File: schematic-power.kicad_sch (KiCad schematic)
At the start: 25 parts, among them IC2 LM76202QPWPRQ1, U9 TPS62933

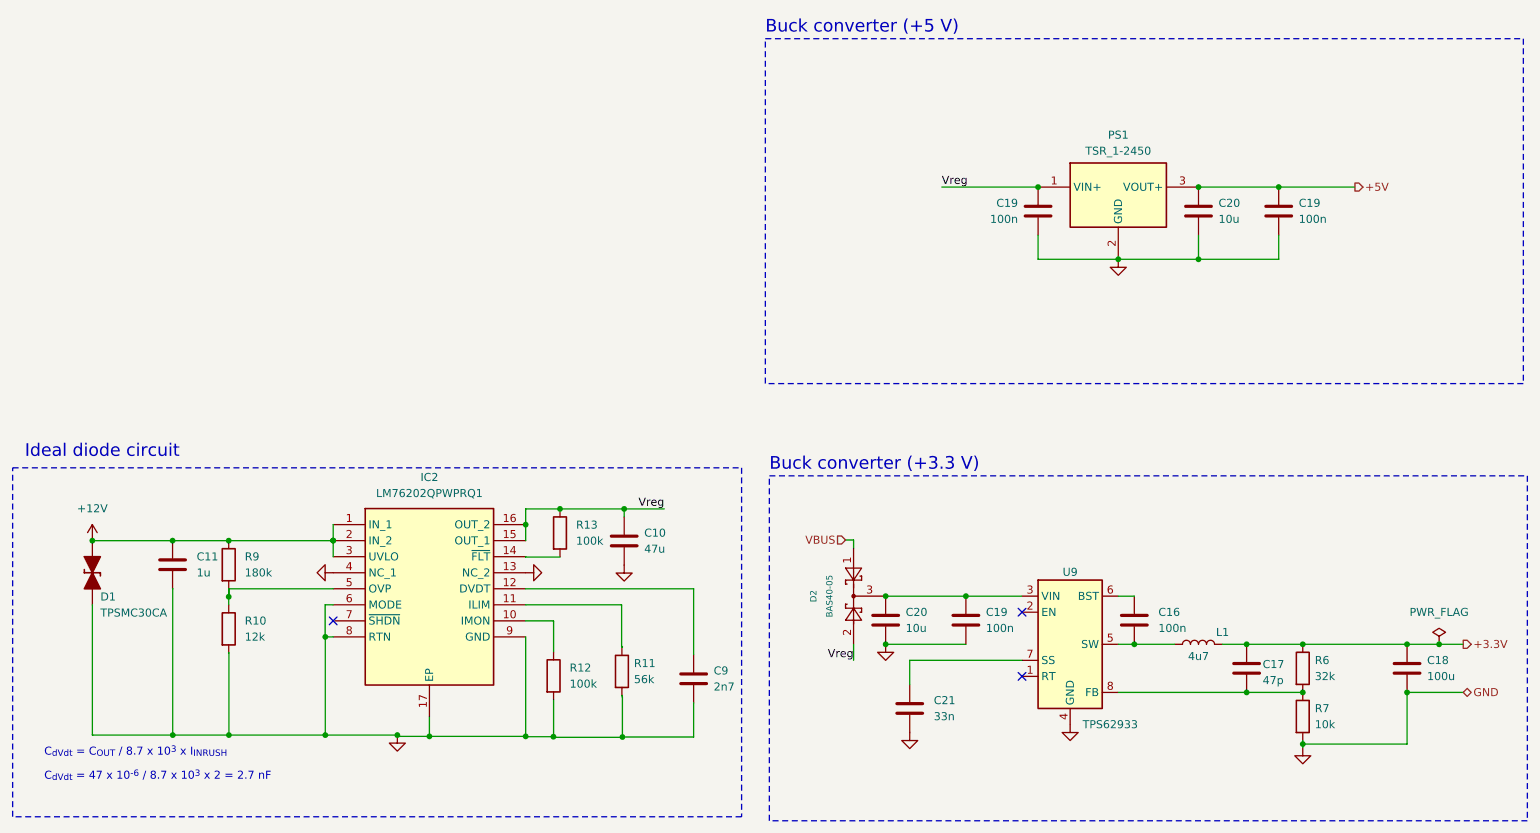
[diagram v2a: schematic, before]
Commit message: Edit mosfets outputs
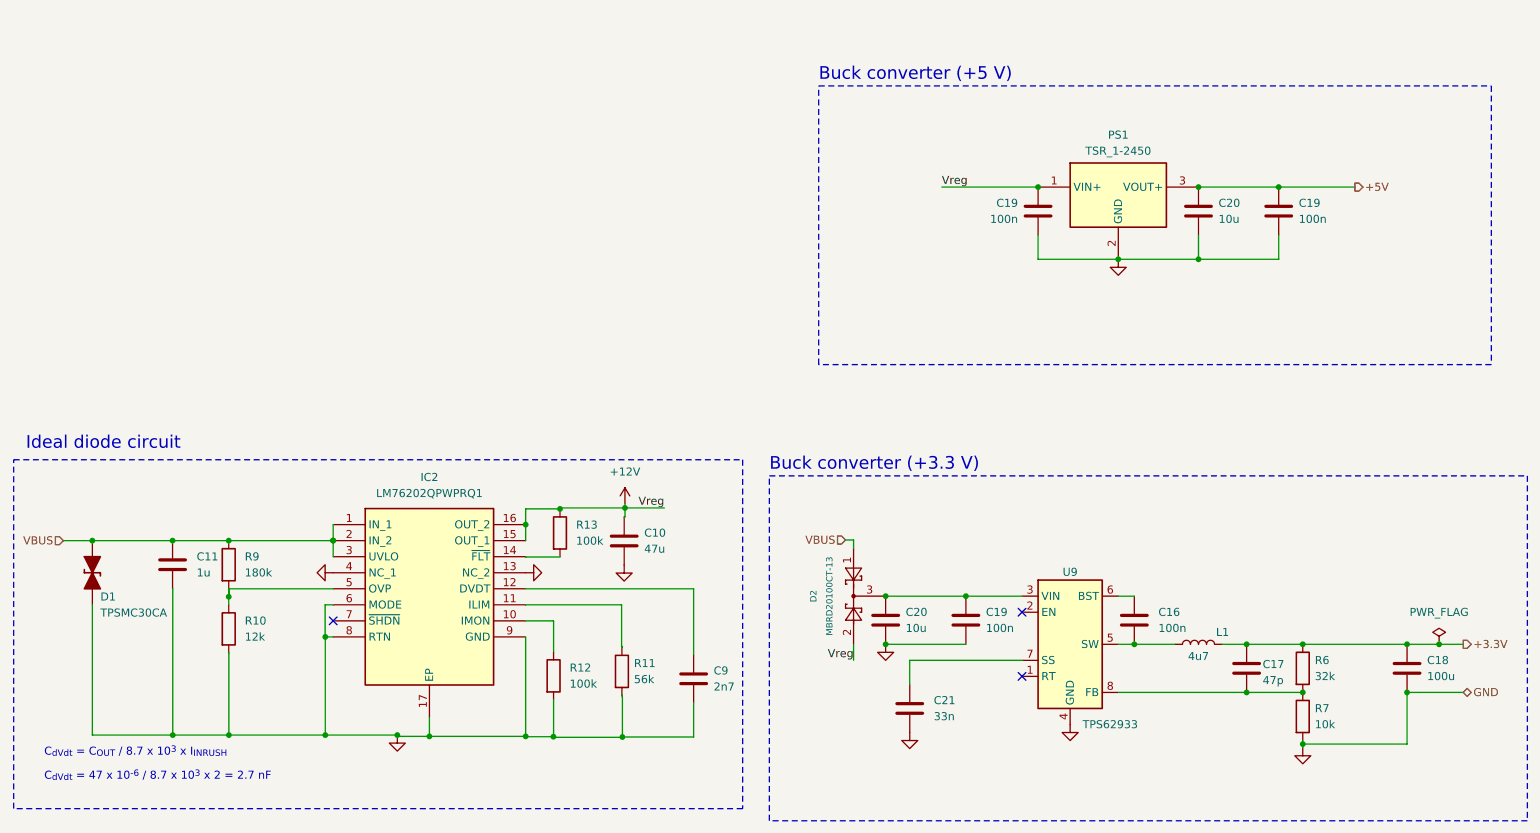
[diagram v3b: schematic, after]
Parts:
- D2: value BAS40-05 -> MBRD20100CT-13; footprint Package_TO_SOT_SMD:SOT-23 -> MBRD20100CT-13:TO252_(DPAK)_1
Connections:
- net Vreg is gone; now on net +12V: C10.1, C19.1, D2.2, IC2.15 (OUT_1), IC2.16 (OUT_2), PS1.1 (VIN+), R13.1
- net +12V: no longer C11.1, D1.2 (A), IC2.1 (IN_1), IC2.2 (IN_2), IC2.3 (UVLO), R9.1
- net VBUS: now also C11.1, D1.2 (A), IC2.1 (IN_1), IC2.2 (IN_2), IC2.3 (UVLO), R9.1
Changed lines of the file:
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@@
   (junction (at 215.9 64.77) (diameter 0) (color 0 0 0 0)
   )
+  (junction (at 203.2 64.77) (diameter 0) (color 0 0 0 0)
+  )
+  (junction (at 62.357 118.2116) (diameter 0) (color 0 0 0 0)
+  )
+  (junction (at 223.52 133.35) (diameter 0) (color 0 0 0 0)
+  )
+  (junction (at 53.467 109.3216) (diameter 0) (color 0 0 0 0)
+  )
+  (junction (at 215.9 53.34) (diameter 0) (color 0 0 0 0)
+  )
+  (junction (at 248.92 133.35) (diameter 0) (color 0 0 0 0)
+  )
+  (junction (at 77.6478 140.1064) (diameter 0) (color 0 0 0 0)
+  )
+  (junction (at 89.0524 140.1064) (diameter 0) (color 0 0 0 0)
+  )
+  (junction (at 78.8924 109.3216) (diameter 0) (color 0 0 0 0)
+  )
+  (junction (at 62.3824 140.1064) (diameter 0) (color 0 0 0 0)
+  )
+  (junction (at 232.41 133.35) (diameter 0) (color 0 0 0 0)
+  )
+  (junction (at 109.3724 106.7816) (diameter 0) (color 0 0 0 0)
+  )
+  (junction (at 190.5 53.34) (diameter 0) (color 0 0 0 0)
+  )
+  (junction (at 166.37 118.11) (diameter 0) (color 0 0 0 0)
+  )
+  (junction (at 205.74 125.73) (diameter 0) (color 0 0 0 0)
+  )
+  (junction (at 124.6886 140.4112) (diameter 0) (color 0 0 0 0)
+  )
+  (junction (at 248.92 125.73) (diameter 0) (color 0 0 0 0)
+  )
   (junction (at 40.767 109.3216) (diameter 0) (color 0 0 0 0)
   )
-  (junction (at 203.2 64.77) (diameter 0) (color 0 0 0 0)
-  )
-  (junction (at 62.357 118.2116) (diameter 0) (color 0 0 0 0)
-  )
-  (junction (at 223.52 133.35) (diameter 0) (color 0 0 0 0)
-  )
-  (junction (at 53.467 109.3216) (diameter 0) (color 0 0 0 0)
-  )
-  (junction (at 215.9 53.34) (diameter 0) (color 0 0 0 0)
-  )
-  (junction (at 248.92 133.35) (diameter 0) (color 0 0 0 0)
-  )
-  (junction (at 77.6478 140.1064) (diameter 0) (color 0 0 0 0)
-  )
-  (junction (at 89.0524 140.1064) (diameter 0) (color 0 0 0 0)
-  )
-  (junction (at 78.8924 109.3216) (diameter 0) (color 0 0 0 0)
-  )
-  (junction (at 62.3824 140.1064) (diameter 0) (color 0 0 0 0)
-  )
-  (junction (at 232.41 133.35) (diameter 0) (color 0 0 0 0)
-  )
-  (junction (at 109.3724 106.7816) (diameter 0) (color 0 0 0 0)
-  )
-  (junction (at 190.5 53.34) (diameter 0) (color 0 0 0 0)
-  )
-  (junction (at 166.37 118.11) (diameter 0) (color 0 0 0 0)
-  )
-  (junction (at 205.74 125.73) (diameter 0) (color 0 0 0 0)
-  )
-  (junction (at 124.6886 140.4112) (diameter 0) (color 0 0 0 0)
-  )
-  (junction (at 248.92 125.73) (diameter 0) (color 0 0 0 0)
-  )
-  (junction (at 124.968 104.2924) (diameter 0) (color 0 0 0 0)
+  (junction (at 125.095 104.14) (diameter 0) (color 0 0 0 0)
   )
   (junction (at 179.07 118.11) (diameter 0) (color 0 0 0 0)
@@
     (stroke (width 0) (type default))
   )
-  (wire (pts (xy 124.968 104.2924) (xy 131.318 104.2924))
+  (wire (pts (xy 125.095 104.14) (xy 131.318 104.14))
     (stroke (width 0) (type default))
   )
@@
     (stroke (width 0) (type default))
   )
+  (wire (pts (xy 125.095 105.5624) (xy 124.968 105.5624))
+    (stroke (width 0) (type default))
+  )
   (wire (pts (xy 124.6886 140.462) (xy 124.6886 140.4112))
     (stroke (width 0) (type default))
@@
     (stroke (width 0) (type default))
   )
+  (wire (pts (xy 125.095 103.505) (xy 125.095 104.14))
+    (stroke (width 0) (type default))
+  )
   (wire (pts (xy 135.9662 116.9416) (xy 109.3724 116.9416))
     (stroke (width 0) (type default))
@@
     (stroke (width 0) (type default))
   )
+  (wire (pts (xy 114.808 104.14) (xy 114.808 104.2924))
+    (stroke (width 0) (type default))
+  )
   (wire (pts (xy 124.6632 134.0612) (xy 124.6632 133.8326))
     (stroke (width 0) (type default))
@@
     (stroke (width 0) (type default))
   )
+  (wire (pts (xy 36.1823 109.3216) (xy 40.767 109.3216))
+    (stroke (width 0) (type default))
+  )
   (wire (pts (xy 240.665 53.34) (xy 228.6 53.34))
     (stroke (width 0) (type default))
@@
     (stroke (width 0) (type default))
   )
-  (wire (pts (xy 114.808 104.2924) (xy 124.968 104.2924))
+  (wire (pts (xy 114.808 104.14) (xy 125.095 104.14))
     (stroke (width 0) (type default))
   )
@@
     (stroke (width 0) (type default))
   )
-  (wire (pts (xy 124.968 105.5624) (xy 124.968 104.2924))
+  (wire (pts (xy 125.095 105.5624) (xy 125.095 104.14))
     (stroke (width 0) (type default))
   )
@@
     (fill (type none))
   )
-  (rectangle (start 28.1432 97.79) (end 143.5608 153.035)
+  (rectangle (start 28.3083 96.5073) (end 143.7259 151.7523)
     (stroke (width 0) (type dash))
     (fill (type none))
   )
-  (rectangle (start 147.32 29.845) (end 267.335 84.455)
+  (rectangle (start 155.7655 37.3253) (end 262.2677 81.4451)
     (stroke (width 0) (type dash))
     (fill (type none))
@@
     (effects (font (size 1.27 1.27)) (justify left bottom))
   )
-  (text "Ideal diode circuit\n" (at 30.0736 96.393 0)
+  (text "Ideal diode circuit\n" (at 30.2387 95.1103 0)
     (effects (font (size 2 2)) (justify left bottom))
   )
@@
     (effects (font (size 2 2)) (justify left bottom))
   )
-  (text "Buck converter (+5 V)" (at 147.32 29.21 0)
+  (text "Buck converter (+5 V)" (at 155.7655 36.6903 0)
     (effects (font (size 2 2)) (justify left bottom))
   )
@@
     (effects (font (size 1.27 1.27)) (justify right bottom))
   )
-  (label "Vreg" (at 131.318 104.2924 180) (fields_autoplaced)
+  (label "Vreg" (at 131.318 104.14 180) (fields_autoplaced)
     (effects (font (size 1.27 1.27)) (justify right bottom))
+  )
+  (hierarchical_label "VBUS" (shape input) (at 36.1823 109.3216 180) (fields_autoplaced)
+    (effects (font (size 1.27 1.27)) (justify right))
   )
   (hierarchical_label "GND" (shape bidirectional) (at 257.81 133.35 0) (fields_autoplaced)
@@
       (effects (font (size 1 1)))
     )
-    (property "Value" "BAS40-05" (at 157.48 118.11 0)
+    (property "Value" "MBRD20100CT-13" (at 157.48 118.11 0)
       (effects (font (size 1 1)))
     )
-    (property "Footprint" "Package_TO_SOT_SMD:SOT-23" (at 156.21 111.76 0)
+    (property "Footprint" "MBRD20100CT-13:TO252_(DPAK)_1" (at 156.21 111.76 0)
       (effects (font (size 1.27 1.27)) (justify left) hide)
     )
@@
     )
   )
-  (symbol (lib_id "power:+12V") (at 40.767 109.3216 0) (unit 1)
-    (in_bom yes) (on_board yes) (dnp no)
-    (property "Reference" "#PWR055" (at 40.767 113.1316 0)
-      (effects (font (size 1.27 1.27)) hide)
-    )
-    (property "Value" "+12V" (at 40.767 104.2416 0)
-      (effects (font (size 1.27 1.27)))
-    )
-    (property "Footprint" "" (at 40.767 109.3216 0)
-      (effects (font (size 1.27 1.27)) hide)
-    )
-    (property "Datasheet" "" (at 40.767 109.3216 0)
-      (effects (font (size 1.27 1.27)) hide)
-    )
-    (pin "1")
-    (instances
-      (project "schematic-main"
-        (path "/c9ad7189-d3b2-414a-9743-efd8e57cd755"
-          (reference "#PWR055") (unit 1)
-        )
-        (path "/c9ad7189-d3b2-414a-9743-efd8e57cd755/ed70203f-44bf-4bdc-8b45-a710eb8fc309"
-          (reference "#PWR054") (unit 1)
-        )
-      )
-    )
-  )
   (symbol (lib_id "Device:C") (at 179.07 121.92 0) (unit 1)
     (in_bom yes) (on_board yes) (dnp no) (fields_autoplaced)
@@
         )
       )
+    )
+  )
+  (symbol (lib_id "power:+12V") (at 125.095 103.505 0) (unit 1)
+    (in_bom yes) (on_board yes) (dnp no)
+    (property "Reference" "#PWR055" (at 125.095 107.315 0)
+      (effects (font (size 1.27 1.27)) hide)
+    )
+    (property "Value" "+12V" (at 125.095 98.425 0)
+      (effects (font (size 1.27 1.27)))
+    )
+    (property "Footprint" "" (at 125.095 103.505 0)
+      (effects (font (size 1.27 1.27)) hide)
+    )
+    (property "Datasheet" "" (at 125.095 103.505 0)
+      (effects (font (size 1.27 1.27)) hide)
+    )
+    (pin "1")
+    (instances
+      (project "schematic-main"
+        (path "/c9ad7189-d3b2-414a-9743-efd8e57cd755"
+          (reference "#PWR055") (unit 1)
+        )
+        (path "/c9ad7189-d3b2-414a-9743-efd8e57cd755/ed70203f-44bf-4bdc-8b45-a710eb8fc309"
+          (reference "#PWR054") (unit 1)
+        )
+      )

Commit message: First pcb
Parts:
- renumbered IC2 to IC1
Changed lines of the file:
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@@
       (project "schematic-main"
         (path "/c9ad7189-d3b2-414a-9743-efd8e57cd755/ed70203f-44bf-4bdc-8b45-a710eb8fc309"
-          (reference "C4") (unit 1)
+          (reference "C8") (unit 1)
         )
       )
@@
   (symbol (lib_id "power:PWR_FLAG") (at 254 125.73 0) (unit 1)
     (in_bom yes) (on_board yes) (dnp no) (fields_autoplaced)
-    (property "Reference" "#FLG03" (at 254 123.825 0)
+    (property "Reference" "#FLG02" (at 254 123.825 0)
       (effects (font (size 1.27 1.27)) hide)
     )
@@
       (project "schematic-main"
         (path "/c9ad7189-d3b2-414a-9743-efd8e57cd755/ed70203f-44bf-4bdc-8b45-a710eb8fc309"
-          (reference "#FLG03") (unit 1)
+          (reference "#FLG02") (unit 1)
         )
       )
@@
       (project "schematic-main"
         (path "/c9ad7189-d3b2-414a-9743-efd8e57cd755/ed70203f-44bf-4bdc-8b45-a710eb8fc309"
-          (reference "#PWR010") (unit 1)
+          (reference "#PWR018") (unit 1)
         )
       )
@@
       (project "schematic-main"
         (path "/c9ad7189-d3b2-414a-9743-efd8e57cd755/ed70203f-44bf-4bdc-8b45-a710eb8fc309"
-          (reference "C9") (unit 1)
+          (reference "C3") (unit 1)
         )
       )
@@
       (project "schematic-main"
         (path "/c9ad7189-d3b2-414a-9743-efd8e57cd755/ed70203f-44bf-4bdc-8b45-a710eb8fc309"
-          (reference "C28") (unit 1)
+          (reference "C11") (unit 1)
         )
       )
@@
       (project "schematic-main"
         (path "/c9ad7189-d3b2-414a-9743-efd8e57cd755/ed70203f-44bf-4bdc-8b45-a710eb8fc309"
-          (reference "R7") (unit 1)
+          (reference "R10") (unit 1)
         )
       )
@@
       (project "schematic-main"
         (path "/c9ad7189-d3b2-414a-9743-efd8e57cd755/ed70203f-44bf-4bdc-8b45-a710eb8fc309"
-          (reference "#PWR087") (unit 1)
+          (reference "#PWR014") (unit 1)
         )
       )
@@
       (project "schematic-main"
         (path "/c9ad7189-d3b2-414a-9743-efd8e57cd755/ed70203f-44bf-4bdc-8b45-a710eb8fc309"
-          (reference "R6") (unit 1)
+          (reference "R8") (unit 1)
         )
       )
@@
       (project "schematic-main"
         (path "/c9ad7189-d3b2-414a-9743-efd8e57cd755/ed70203f-44bf-4bdc-8b45-a710eb8fc309"
-          (reference "C6") (unit 1)
+          (reference "C10") (unit 1)
         )
       )
@@
       (project "schematic-main"
         (path "/c9ad7189-d3b2-414a-9743-efd8e57cd755/ed70203f-44bf-4bdc-8b45-a710eb8fc309"
-          (reference "#PWR088") (unit 1)
+          (reference "#PWR012") (unit 1)
         )
       )
@@
       (project "schematic-main"
         (path "/c9ad7189-d3b2-414a-9743-efd8e57cd755/ed70203f-44bf-4bdc-8b45-a710eb8fc309"
-          (reference "C5") (unit 1)
+          (reference "C2") (unit 1)
         )
       )
@@
       (project "schematic-main"
         (path "/c9ad7189-d3b2-414a-9743-efd8e57cd755/ed70203f-44bf-4bdc-8b45-a710eb8fc309"
-          (reference "R11") (unit 1)
+          (reference "R7") (unit 1)
         )
       )
@@
       (project "schematic-main"
         (path "/c9ad7189-d3b2-414a-9743-efd8e57cd755/ed70203f-44bf-4bdc-8b45-a710eb8fc309"
-          (reference "#PWR053") (unit 1)
+          (reference "#PWR020") (unit 1)
         )
       )
@@
       (project "schematic-main"
         (path "/c9ad7189-d3b2-414a-9743-efd8e57cd755/ed70203f-44bf-4bdc-8b45-a710eb8fc309"
-          (reference "#PWR09") (unit 1)
+          (reference "#PWR019") (unit 1)
         )
       )
@@
       (project "schematic-main"
         (path "/c9ad7189-d3b2-414a-9743-efd8e57cd755/ed70203f-44bf-4bdc-8b45-a710eb8fc309"
-          (reference "#PWR07") (unit 1)
+          (reference "#PWR015") (unit 1)
         )
       )
@@
       (project "schematic-main"
         (path "/c9ad7189-d3b2-414a-9743-efd8e57cd755/ed70203f-44bf-4bdc-8b45-a710eb8fc309"
-          (reference "C27") (unit 1)
+          (reference "C9") (unit 1)
         )
       )
@@
       (project "schematic-main"
         (path "/c9ad7189-d3b2-414a-9743-efd8e57cd755/ed70203f-44bf-4bdc-8b45-a710eb8fc309"
-          (reference "C2") (unit 1)
+          (reference "C4") (unit 1)
         )
       )
@@
       (project "schematic-main"
         (path "/c9ad7189-d3b2-414a-9743-efd8e57cd755/ed70203f-44bf-4bdc-8b45-a710eb8fc309"
-          (reference "#PWR012") (unit 1)
+          (reference "#PWR013") (unit 1)
         )
       )
@@
       (project "schematic-main"
         (path "/c9ad7189-d3b2-414a-9743-efd8e57cd755/ed70203f-44bf-4bdc-8b45-a710eb8fc309"
-          (reference "C7") (unit 1)
+          (reference "C12") (unit 1)
         )
       )
@@
       (project "schematic-main"
         (path "/c9ad7189-d3b2-414a-9743-efd8e57cd755/ed70203f-44bf-4bdc-8b45-a710eb8fc309"
-          (reference "#PWR011") (unit 1)
+          (reference "#PWR021") (unit 1)
         )
       )
@@
   (symbol (lib_id "Lm7602 ideal diode:LM76202QPWPRQ1") (at 78.8924 106.7816 0) (unit 1)
     (in_bom yes) (on_board yes) (dnp no) (fields_autoplaced)
-    (property "Reference" "IC2" (at 94.1324 99.2886 0)
+    (property "Reference" "IC1" (at 94.1324 99.2886 0)
       (effects (font (size 1.27 1.27)))
     )
@@
       (project "schematic-main"
         (path "/c9ad7189-d3b2-414a-9743-efd8e57cd755/ed70203f-44bf-4bdc-8b45-a710eb8fc309"
-          (reference "IC2") (unit 1)
+          (reference "IC1") (unit 1)
         )
       )
@@
       (project "schematic-main"
         (path "/c9ad7189-d3b2-414a-9743-efd8e57cd755/ed70203f-44bf-4bdc-8b45-a710eb8fc309"
-          (reference "C3") (unit 1)
+          (reference "C6") (unit 1)
         )
       )
@@
       (project "schematic-main"
         (path "/c9ad7189-d3b2-414a-9743-efd8e57cd755/ed70203f-44bf-4bdc-8b45-a710eb8fc309"
-          (reference "U2") (unit 1)
+          (reference "U1") (unit 1)
         )
       )
@@
       (project "schematic-main"
         (path "/c9ad7189-d3b2-414a-9743-efd8e57cd755/ed70203f-44bf-4bdc-8b45-a710eb8fc309"
-          (reference "C8") (unit 1)
+          (reference "C5") (unit 1)
         )
       )
@@
       (project "schematic-main"
         (path "/c9ad7189-d3b2-414a-9743-efd8e57cd755/ed70203f-44bf-4bdc-8b45-a710eb8fc309"
-          (reference "R8") (unit 1)
+          (reference "R6") (unit 1)
         )
       )
@@
       (project "schematic-main"
         (path "/c9ad7189-d3b2-414a-9743-efd8e57cd755/ed70203f-44bf-4bdc-8b45-a710eb8fc309"
-          (reference "C29") (unit 1)
+          (reference "C7") (unit 1)
         )
       )
@@
       (project "schematic-main"
         (path "/c9ad7189-d3b2-414a-9743-efd8e57cd755/ed70203f-44bf-4bdc-8b45-a710eb8fc309"
-          (reference "R10") (unit 1)
+          (reference "R9") (unit 1)
         )
       )
@@
         )
         (path "/c9ad7189-d3b2-414a-9743-efd8e57cd755/ed70203f-44bf-4bdc-8b45-a710eb8fc309"
-          (reference "#PWR054") (unit 1)
+          (reference "#PWR016") (unit 1)
         )
       )
@@
       (project "schematic-main"
         (path "/c9ad7189-d3b2-414a-9743-efd8e57cd755/ed70203f-44bf-4bdc-8b45-a710eb8fc309"
-          (reference "#PWR06") (unit 1)
+          (reference "#PWR017") (unit 1)
         )
       )
@@
       (project "schematic-main"
         (path "/c9ad7189-d3b2-414a-9743-efd8e57cd755/ed70203f-44bf-4bdc-8b45-a710eb8fc309"
-          (reference "R9") (unit 1)
-        )
-      )
+          (reference "R11") (unit 1)
+        )
+      )

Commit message: PCB design 80%
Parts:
- PS1: footprint TSR-1-24120 -> Lib:TSR-1-24120
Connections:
- net VBUS: no longer C11.1, D1.2 (A), IC1.1 (IN_1), IC1.2 (IN_2), IC1.3 (UVLO), R9.1
- new net Vin: C11.1, D1.2 (A), IC1.1 (IN_1), IC1.2 (IN_2), IC1.3 (UVLO), R9.1
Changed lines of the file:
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@@
 		)
 	)
-	(hierarchical_label "VBUS"
+	(hierarchical_label "Vin"
 		(shape input)
 		(at 36.1823 109.3216 180)
@@
 			)
 		)
-		(property "Footprint" "TSR-1-24120"
+		(property "Footprint" "Lib:TSR-1-24120"
 			(at 212.09 146.99 0)
 			(effects
